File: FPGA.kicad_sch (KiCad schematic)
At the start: 53 parts, among them IC10 ICE5LP4K-SG48I, IC11 MT25QL128ABA1ESE-0SIT, J12 SAMTEC_TSW-101-23-L-D, J13 SAMTEC_TSW-105-23-L-D, J14 SAMTEC_TSW-101-23-L-D, J15 SAMTEC_SSW-106-02-L-D-RA, J16 SAMTEC_SSW-106-02-L-D-RA, J19 SAMTEC_TSW-102-23-L-D, SW4 HARWIN_M50-1900005, SW5 HARWIN_M50-1900005, SW6 HARWIN_M50-1900005, SW7 HARWIN_M50-1900005

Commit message: Updated schematic after routing, added layout
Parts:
- removed C? (x13): CC0603_100NF_50V_10%_X7R, Capacitors SMD:CAPC1608X87N, symbol Capacitors SMD:CC0603_100NF_50V_10%_X7R
- removed C? (x6): CC0603_10UF_25V_20%_X5R, Capacitors SMD:CAPC1709X100N, symbol Capacitors SMD:CC0603_10UF_25V_20%_X5R
- removed D10, D7: PESD3V3L5UY, ICs And Semiconductors SMD:SOT65P210X110-6N, symbol Diodes:PESD3V3L5UY
- removed D11: 1N4148WS, ICs And Semiconductors SMD:SODFL2512X100N, symbol Diodes:1N4148WS
- removed D? (x3): SMBJ3V3, ICs And Semiconductors SMD:DIOM5436X244N, symbol Diodes:SMBJ3V3
- removed IC10: ICE5LP4K-SG48I, ICs And Semiconductors SMD:QFN50P700X700X100-49N-S550, symbol Logic:ICE5LP4K-SG48I
- removed IC11: MT25QL128ABA1ESE-0SIT, ICs And Semiconductors SMD:SOIC127P790X216-8N, symbol Logic:MT25QL128ABA1ESE-0SIT
- removed J12, J14: SAMTEC_TSW-101-23-L-D, SAMTEC THD:SAMTEC_TSW-101-23-L-D, symbol SAMTEC:SAMTEC_TSW-101-23-L-D
- removed J13: SAMTEC_TSW-105-23-L-D, SAMTEC THD:SAMTEC_TSW-105-23-L-D, symbol SAMTEC:SAMTEC_TSW-105-23-L-D
- removed J15, J16: SAMTEC_SSW-106-02-L-D-RA, SAMTEC THD:SAMTEC_SSW-106-02-L-D-RA, symbol SAMTEC:SAMTEC_SSW-106-02-L-D-RA
- removed J19: SAMTEC_TSW-102-23-L-D, SAMTEC THD:SAMTEC_TSW-102-23-L-D, symbol SAMTEC:SAMTEC_TSW-102-23-L-D
- removed OSC?: OSC_100MHZ_IQD_LFSPXO022731, ICs And Semiconductors SMD:OSC_IQD_CFPS-73, symbol Crystals & Oscillators:OSC_100MHZ_IQD_LFSPXO022731
- removed R37, R38, R39, R40: R0603_10K_1%_0.1W_100PPM, Resistors SMD:RESC1608X55N, symbol Resistors SMD:R0603_10K_1%_0.1W_100PPM
- removed R41: R0603_100R_1%_0.1W_100PPM, Resistors SMD:RESC1608X55N, symbol Resistors SMD:R0603_100R_1%_0.1W_100PPM
- removed R43, R44, R45: R0603_2K2_1%_0.1W_100PPM, Resistors SMD:RESC1608X55N, symbol Resistors SMD:R0603_2K2_1%_0.1W_100PPM
- removed R? (x2): R0603_4K7_1%_0.1W_100PPM, Resistors SMD:RESC1608X55N, symbol Resistors SMD:R0603_4K7_1%_0.1W_100PPM
- removed R?: R0603_1K_1%_0.1W_100PPM, Resistors SMD:RESC1608X55N, symbol Resistors SMD:R0603_1K_1%_0.1W_100PPM
- removed SW4, SW5, SW6, SW7: HARWIN_M50-1900005, symbol HARWIN:HARWIN_M50-1900005
- removed TP? (x2): SMD_PAD_1.27X1.27MM, Pads:TPS127, symbol Pads:SMD_PAD_1.27X1.27MM
- added C76, C77, C78, C83, C84, C85, C86, C87, C88, C89, C90, C91, C94: CC0603_100NF_50V_10%_X7R, Capacitors SMD:CAPC1608X87N, symbol Capacitors SMD:CC0603_100NF_50V_10%_X7R
- added C79, C80, C81, C82, C92, C93: CC0603_10UF_25V_20%_X5R, Capacitors SMD:CAPC1709X100N, symbol Capacitors SMD:CC0603_10UF_25V_20%_X5R
- added D11, D14: PESD3V3L5UY, ICs And Semiconductors SMD:SOT65P210X110-6N, symbol Diodes:PESD3V3L5UY
- added D12, D13, D16: PESD3V3S1UB, ICs And Semiconductors SMD:SODFL1608X65N, symbol Diodes:PESD3V3S1UB
- added D15: 1N4148WS, ICs And Semiconductors SMD:SODFL2512X100N, symbol Diodes:1N4148WS
- added IC17: ICE5LP4K-SG48I, ICs And Semiconductors SMD:QFN50P700X700X100-49N-S550, symbol Logic:ICE5LP4K-SG48I
- added IC18: MT25QL128ABA1ESE-0SIT, ICs And Semiconductors SMD:SOIC127P790X216-8N, symbol Logic:MT25QL128ABA1ESE-0SIT
- added J13: SAMTEC_HTSW-102-23-L-D, SAMTEC THD:SAMTEC_HTSW-102-23-L-D, symbol SAMTEC:SAMTEC_HTSW-102-23-L-D
- added J14, J16: SAMTEC_HTSW-101-23-L-D, SAMTEC THD:SAMTEC_HTSW-101-23-L-D, symbol SAMTEC:SAMTEC_HTSW-101-23-L-D
- added J15: SAMTEC_HTSW-105-23-L-D, SAMTEC THD:SAMTEC_HTSW-105-23-L-D, symbol SAMTEC:SAMTEC_HTSW-105-23-L-D
- added J17, J18: SAMTEC_SSW-106-02-L-D-RA, SAMTEC THD:SAMTEC_SSW-106-02-L-D-RA, symbol SAMTEC:SAMTEC_SSW-106-02-L-D-RA
- added OSC2: OSC_100MHZ_IQD_LFSPXO022731, ICs And Semiconductors SMD:OSC_IQD_CFPS-73, symbol Crystals & Oscillators:OSC_100MHZ_IQD_LFSPXO022731
- added R52, R53: R0603_4K7_1%_0.1W_100PPM, Resistors SMD:RESC1608X55N, symbol Resistors SMD:R0603_4K7_1%_0.1W_100PPM
- added R54, R55, R56, R57: R0603_10K_1%_0.1W_100PPM, Resistors SMD:RESC1608X55N, symbol Resistors SMD:R0603_10K_1%_0.1W_100PPM
- added R58: R0603_100R_1%_0.1W_100PPM, Resistors SMD:RESC1608X55N, symbol Resistors SMD:R0603_100R_1%_0.1W_100PPM
- added R59: R0603_1K_1%_0.1W_100PPM, Resistors SMD:RESC1608X55N, symbol Resistors SMD:R0603_1K_1%_0.1W_100PPM
- added R60, R61, R62: R0603_2K2_1%_0.1W_100PPM, Resistors SMD:RESC1608X55N, symbol Resistors SMD:R0603_2K2_1%_0.1W_100PPM
- added SW10, SW11, SW8, SW9: HARWIN_M50-1900005, COMATEL THD:STELVIO-KONTEK_3131730000400, symbol STELVIO-KONTEK COMATEL:STELVIO-KONTEK_3131730000400
- added TP39, TP40: HARWIN_S1751-46, HARWIN SMD:HARWIN_S1751-46, symbol HARWIN:HARWIN_S1751-46
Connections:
- net +1V2: now also C81.1, C82.1, C84.1, C85.1, IC17.30 (VCC), IC17.5 (VCC), R58.2
- net +2V5: now also C79.1, C86.1, IC17.24 (VPP_2V5)
- net +3V3D: now also C76.1, C77.1, C78.1, C87.1, C88.1, C89.1, C90.1, C91.1, C92.1, C93.1, C94.1, IC17.1 (VCCIO_2), IC17.22 (SPI_Vccio1), IC17.33 (VCCIO_0), IC18.8 (VCC), J17.1, J17.2, J18.1, J18.2, OSC2.1 (E), OSC2.4 (+Vs), R52.2, R53.2, R54.2, R55.2, R56.2, R57.2, R59.1
- net ACCURATE_RESET: now also IC17.34 (IOT_44b)
- net Comp1: now also IC17.26 (IOT_39a)
- net Comp2: now also IC17.27 (IOT_38b)
- net Comp3: now also IC17.23 (IOT_37a)
- net Comp4: now also IC17.25 (IOT_36b)
- net Enable.High: now also IC17.28 (IOT_41a)
- net Enable.Low: now also IC17.32 (IOT_43a)
- net Enable.Medium: now also IC17.31 (IOT_42b)
- net FLASH_MISO: now also D11.4 (C), D14.1 (C), IC18.2 (DQ1), J13.3, J15.5, SW9.1
- net FLASH_MOSI: now also D11.3 (C), D14.5 (C), IC18.5 (DQ0), J13.2, J15.8
- net FPGA_CLK: now also IC17.37 (IOT_45a_G1)
- net FPGA_PROG0: now also D14.3 (C), IC17.15 (IOB_34a_SPI_SCK), IC18.6 (C), J15.7, R57.1
- net FPGA_PROG4: now also D12.1 (C), D14.4 (C), IC17.16 (IOB_35b_SPI_SS), J14.2, J15.9, SW10.1
- net FPGA_PROG6: now also D16.1 (C), IC17.7 (CDONE), J16.1
- net FPGA_PROG7: now also D15.1 (C), IC17.8 (creset_b)
- net FPGA_RX: now also IC17.42 (IOT_51a)
- net FPGA_SCL: now also IC17.43 (IOT_49a), R53.1, TP40.1
- net FPGA_SDA: now also IC17.36 (IOT_48b), R52.1, TP39.1
- net FPGA_TX: now also IC17.38 (IOT_50b)
- net GND: now also C76.2, C77.2, C78.2, C79.2, C80.2, C81.2, C82.2, C83.2, C84.2, C85.2, C86.2, C87.2, C88.2, C89.2, C90.2, C91.2, C92.2, C93.2, C94.2, D11.2 (A), D11.2 (A), D11.2 (A), D11.2 (A), D11.2 (A), D12.2 (A), D13.2 (A), D14.2 (A), D14.2 (A), D14.2 (A), D14.2 (A), D14.2 (A), D16.2 (A), IC17.49 (EP), IC18.4 (VSS), J15.10, J15.2, J17.3, J17.4, J18.3, J18.4, OSC2.2 (GND)
- net IOB_0: now also IC17.46 (IOB_0a), J17.12
- net IOB_13: now also IC17.6 (IOB_13b), J18.12
- net IOB_16: now also IC17.9 (IOB_16a), J18.10
- net IOB_18: now also IC17.10 (IOB_18a), J18.8
- net IOB_2: now also IC17.47 (IOB_2a), J17.10
- net IOB_20: now also IC17.11 (IOB_20a), J18.6
- net IOB_22: now also IC17.12 (IOB_22a), J18.11
- net IOB_23: now also IC17.21 (IOB_23b), J18.9
- net IOB_24: now also IC17.13 (IOB_24a), J18.7
- net IOB_25: now also IC17.20 (IOB_25b_G3), J18.5
- net IOB_3: now also IC17.44 (IOB_3b_G6), J17.8
- net IOB_4: now also IC17.48 (IOB_4a), J17.6
- net IOB_5: now also IC17.45 (IOB_5b), J17.11
- net IOB_6: now also IC17.2 (IOB_6a), J17.9
- net IOB_8: now also IC17.4 (IOB_8a), J17.7
- net IOB_9: now also IC17.3 (IOB_9b), J17.5
- net RESET: now also D15.2 (A)
- net RGB0: now also IC17.41 (RGB0), R60.1
- net RGB1: now also IC17.40 (RGB1), R61.1
- net RGB2: now also IC17.39 (RGB2), R62.1
- net SERCOM1: now also IC17.19 (IOB_29b)
- net SERCOM2: now also IC17.18 (IOB_31b)
- net iCE_CDONE_PullUp: now also J16.2, R59.2, SW11.1
- net iCE_CLK: now also IC17.35 (IOT_46b_G0), OSC2.3 (OUT)
- net iCE_MISO: now also D11.5 (C), IC17.14 (IOB_32a_SPI_SO), J13.4
- net iCE_MOSI: now also D11.1 (C), IC17.17 (IOB_33b_SPI_SI), J13.1, SW8.1
- net at LD13.3 (CG): now also R61.2
- net at LD13.2 (CB): now also R60.2
- net at LD13.4 (CR): now also R62.2
- new net: D13.1 (C), IC18.1 (~{S}), J14.1, R56.1
- new net: C80.1, C83.1, IC17.29 (VCCPLL), R58.1
- new net: IC18.3 (~{W/}DQ2), R55.1
- new net: IC18.7 (~{HOLD/}DQ3), R54.1
- no-connect marks 10 -> 6

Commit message: Annotation now matches the produced PCB
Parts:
- renumbered C76 to C41, C77 to C42, C78 to C43, C86 to C44, C80 to C45, C83 to C46, C88 to C47, C92 to C48, C93 to C49, C87 to C50, C91 to C51, C89 to C52, C90 to C53, C94 to C54, C84 to C90, C81 to C91, C82 to C92, C85 to C93, C79 to C94, D14 to D10, D15 to D11, D16 to D12, D11 to D7, D12 to D8, D13 to D9, IC17 to IC10, IC18 to IC11, J13 to J11, J14 to J12, J15 to J13, J16 to J14, J17 to J15, J18 to J16, R52 to R35, R53 to R36, R54 to R37, R55 to R38, R56 to R39, R57 to R40, R58 to R41, R59 to R42, R60 to R43, R61 to R44, R62 to R45, SW8 to SW4, SW9 to SW5, SW10 to SW6, SW11 to SW7, TP39 to TP16, TP40 to TP17

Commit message: Fixed reset circuits, removed 1V2 LED, fixing 2V5 circuit, added pullups to FPGA I2C, moved PSU TPs and JMPrs, replaced OSC2, removed ADC, added 2232 DTR, removed PSU seq TPs, replaced 2V5 LED res
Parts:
- removed D11: 1N4148WS, ICs And Semiconductors SMD:SODFL2512X100N, symbol Diodes:1N4148WS
- removed D12: PESD3V3S1UB, ICs And Semiconductors SMD:SODFL1608X65N, symbol Diodes:PESD3V3S1UB
- removed LD12: LED_LITEON_LTST-C193KGKT-5A, ICs And Semiconductors SMD:LED_LITEON_LTST-C193KGKT-5A, symbol LEDs & Displays:LED_LITEON_LTST-C193KGKT-5A
- removed OSC2: OSC_100MHZ_IQD_LFSPXO022731, ICs And Semiconductors SMD:OSC_IQD_CFPS-73, symbol Crystals & Oscillators:OSC_100MHZ_IQD_LFSPXO022731
- removed R42: R0603_1K_1%_0.1W_100PPM, Resistors SMD:RESC1608X55N, symbol Resistors SMD:R0603_1K_1%_0.1W_100PPM
- removed SW7: HARWIN_M50-1900005, COMATEL THD:STELVIO-KONTEK_3131730000400, symbol STELVIO-KONTEK COMATEL:STELVIO-KONTEK_3131730000400
- removed TP16, TP17: HARWIN_S1751-46, HARWIN SMD:HARWIN_S1751-46, symbol HARWIN:HARWIN_S1751-46
- added LD5: LED_LITEON_LTST-C193KGKT-5A, ICs And Semiconductors SMD:LED_LITEON_LTST-C193KGKT-5A, symbol LEDs & Displays:LED_LITEON_LTST-C193KGKT-5A
- added OSC2: OSC_100MHZ_ABRACON_ASFL1-100.000MHZ-EC, ICs And Semiconductors SMD:OSC_ABRACON_ASFL1, symbol Crystals & Oscillators:OSC_100MHZ_ABRACON_ASFL1-100.000MHZ-EC
- added R13: R0603_1K_1%_0.1W_100PPM, Resistors SMD:RESC1608X55N, symbol Resistors SMD:R0603_1K_1%_0.1W_100PPM
- added R42: R0603_10K_1%_0.1W_100PPM, Resistors SMD:RESC1608X55N, symbol Resistors SMD:R0603_10K_1%_0.1W_100PPM
- R35, R36: now fitted
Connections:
- net iCE_CDONE_PullUp is gone; now on net FPGA_PROG7: J14.2
- net +3V3D: now also OSC2.1 (OE), OSC2.4 (VDD), R13.1, R42.1
- net FPGA_PROG6: now also LD5.2 (A), R13.2; no longer J14.1
- net FPGA_PROG7: now also R42.2
- net GND: now also J14.1, LD5.1 (C), OSC2.2 (GND)
- net iCE_CLK: now also OSC2.3 (OUT)
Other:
- note removed: "CDONE Status LED"
- moved on the sheet: C50, C54

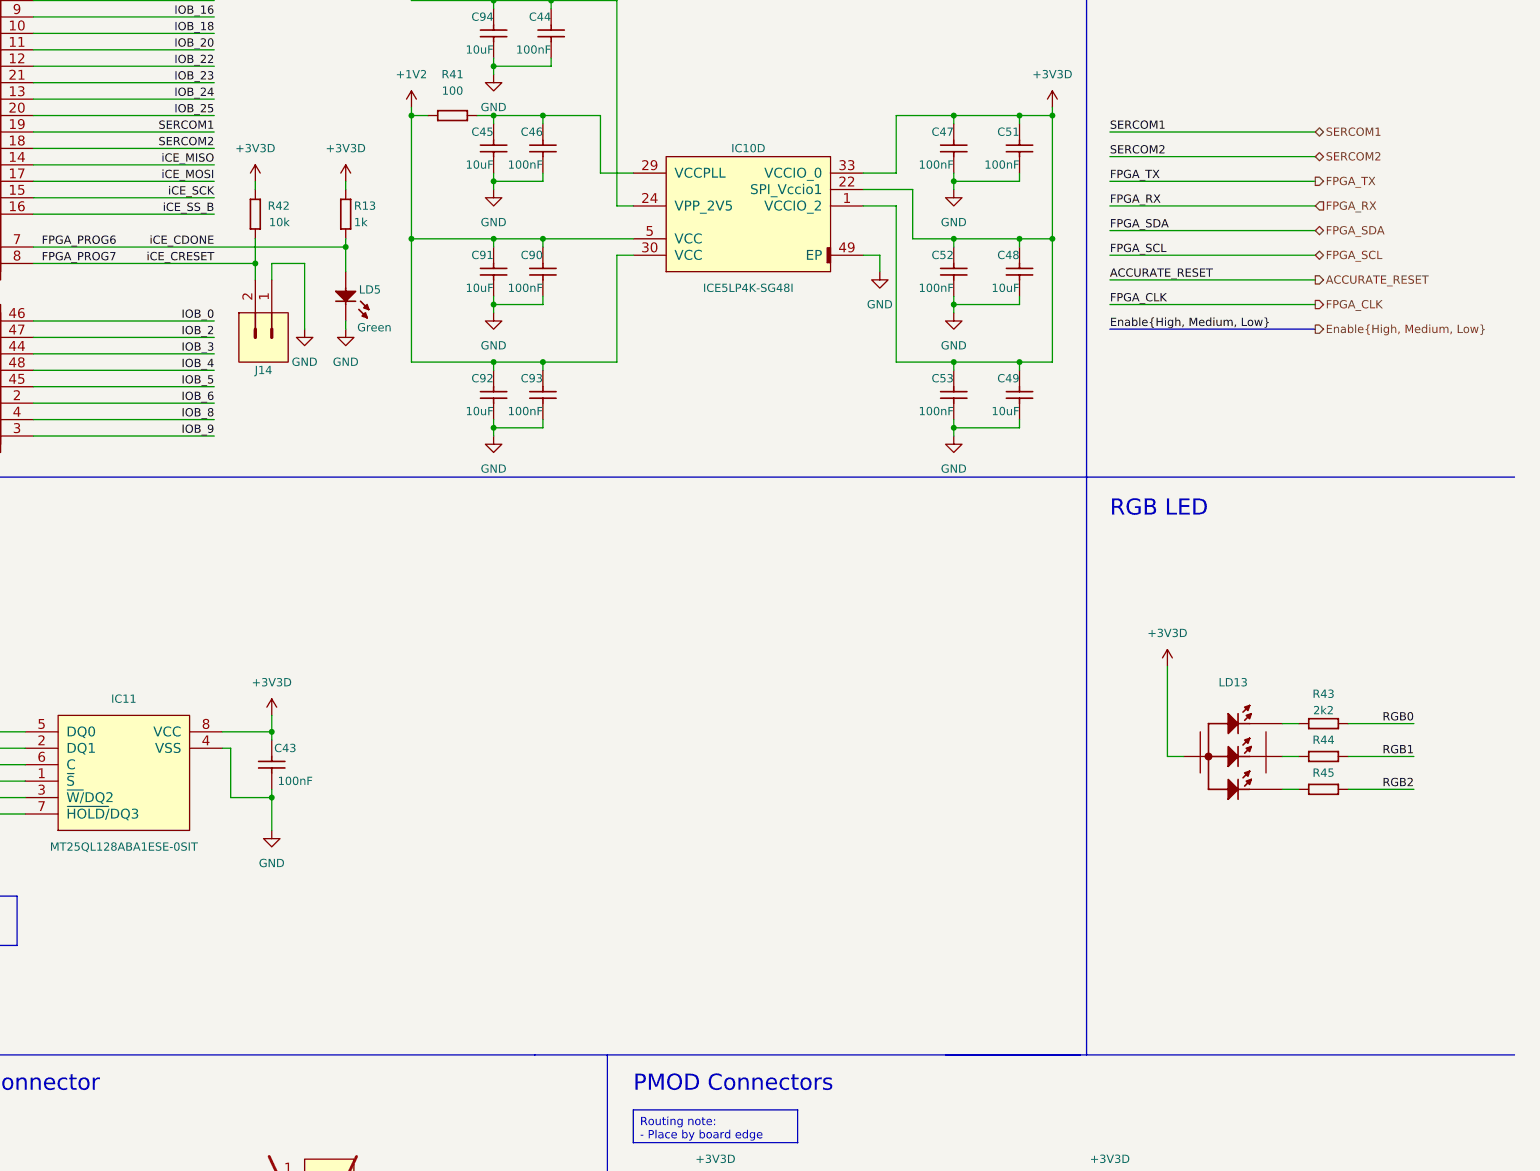
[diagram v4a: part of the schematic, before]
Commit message: Added FPGA reset button, renamed SERCOM
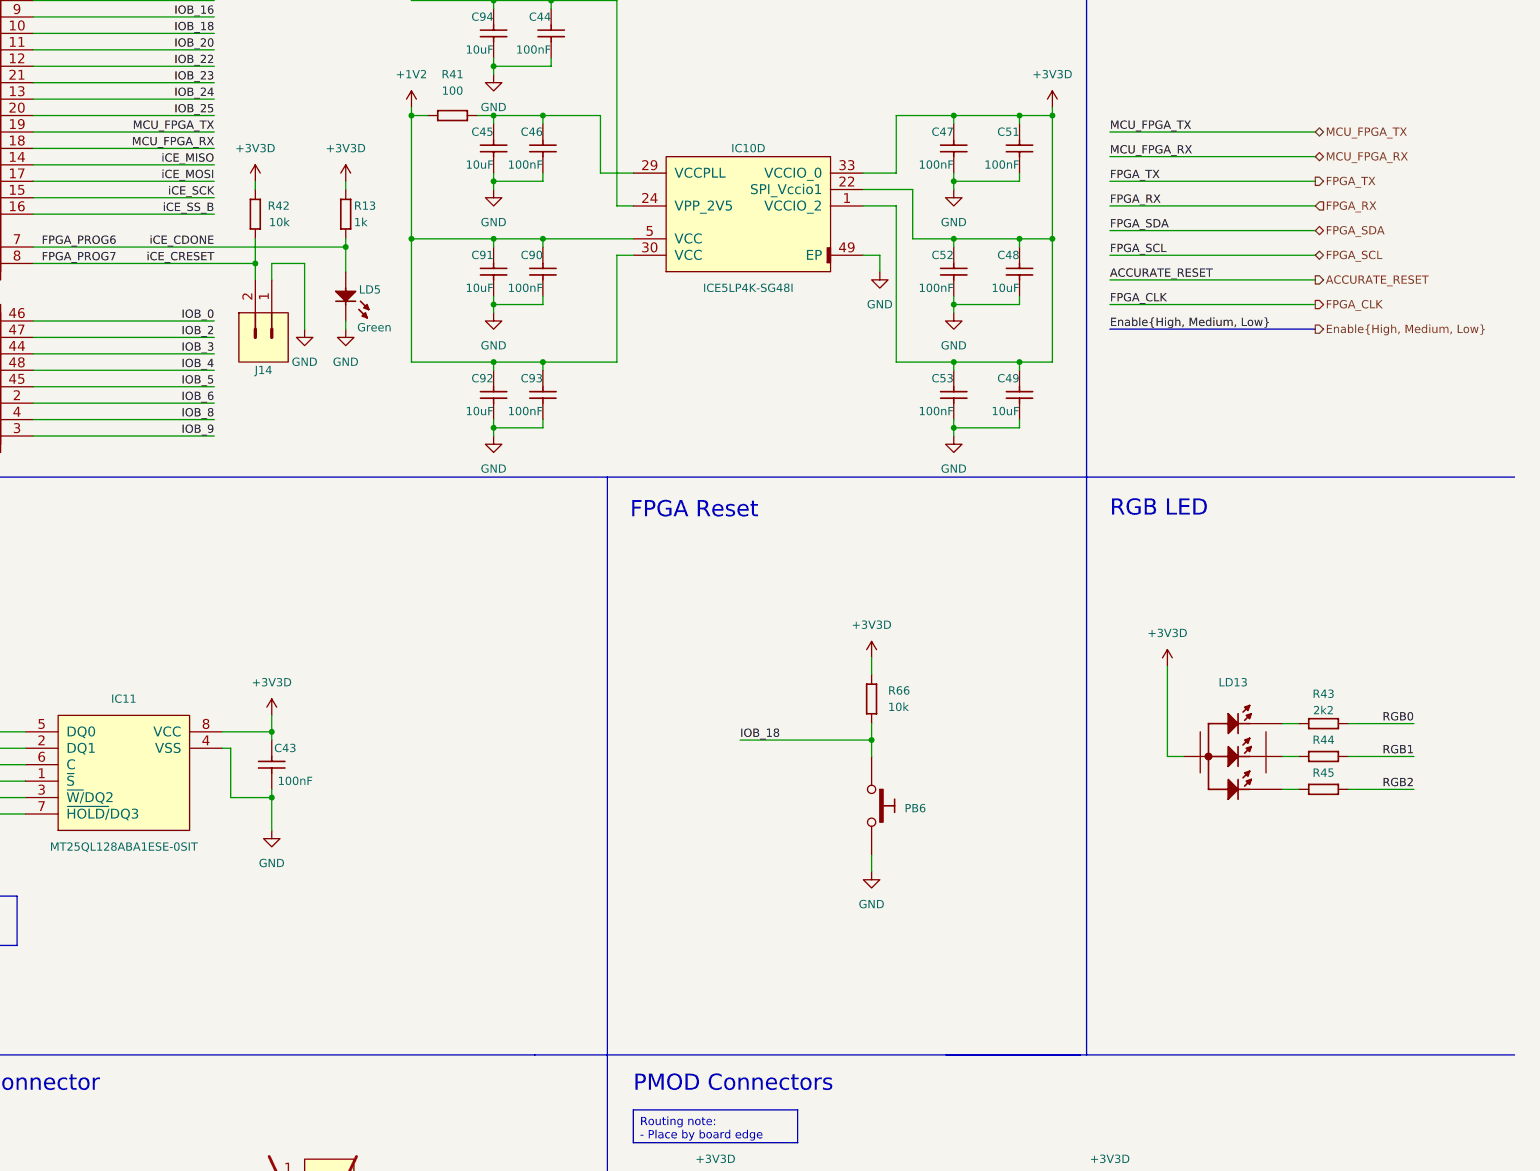
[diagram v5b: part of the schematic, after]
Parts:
- added PB6: PB_C&K_KSC321JLFS, Switches:PB_C&K_KSC321J, symbol Switches:PB_C&K_KSC321JLFS
- added R66: R0603_10K_1%_0.1W_100PPM, Resistors SMD:RESC1608X55N, symbol Resistors SMD:R0603_10K_1%_0.1W_100PPM
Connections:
- net +3V3D: now also R66.1
- net GND: now also PB6.3, PB6.4
- net IOB_18: now also PB6.1, PB6.2, R66.2
- net SERCOM1 renamed MCU_FPGA_TX
- net SERCOM2 renamed MCU_FPGA_RX
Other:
- note added: "FPGA Reset"

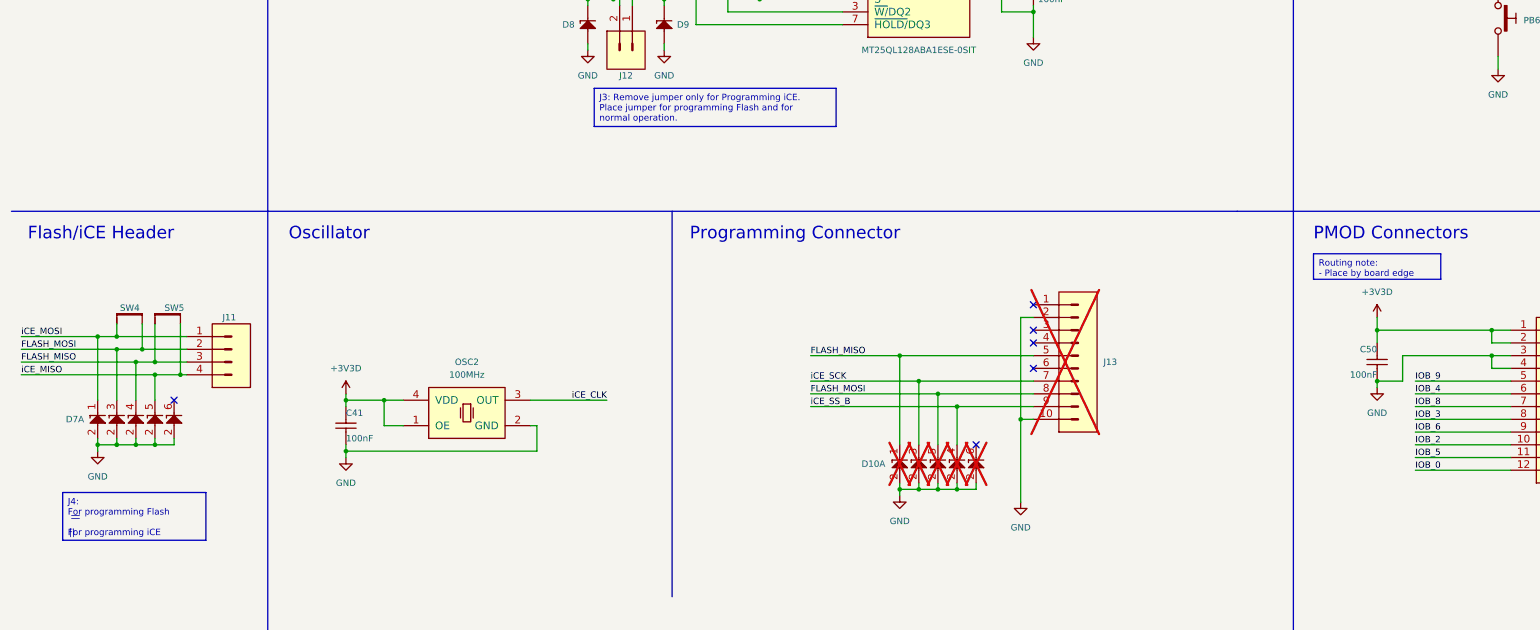
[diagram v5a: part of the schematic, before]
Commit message: Rename Power Supply sheet, remove iCE programming option
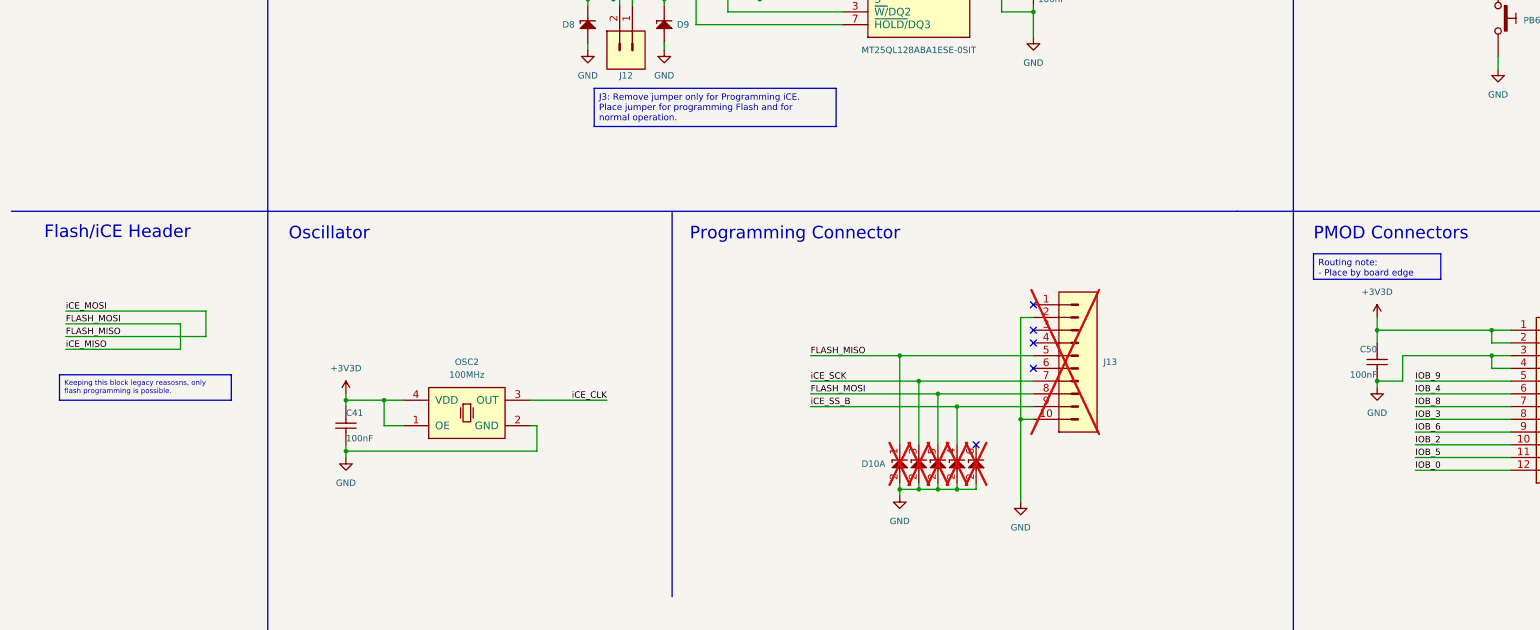
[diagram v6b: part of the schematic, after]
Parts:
- removed D7: PESD3V3L5UY, ICs And Semiconductors SMD:SOT65P210X110-6N, symbol Diodes:PESD3V3L5UY
- removed J11: SAMTEC_HTSW-102-23-L-D, SAMTEC THD:SAMTEC_HTSW-102-23-L-D, symbol SAMTEC:SAMTEC_HTSW-102-23-L-D
- removed SW4, SW5: HARWIN_M50-1900005, COMATEL THD:STELVIO-KONTEK_3131730000400, symbol STELVIO-KONTEK COMATEL:STELVIO-KONTEK_3131730000400
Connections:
- net iCE_MISO is gone; now on net FLASH_MOSI: IC10.14 (IOB_32a_SPI_SO)
- net iCE_MOSI is gone; now on net FLASH_MISO: IC10.17 (IOB_33b_SPI_SI)
- no-connect marks 6 -> 5
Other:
- note removed: "||"
